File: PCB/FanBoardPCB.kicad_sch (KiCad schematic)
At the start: 0 parts

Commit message: yippeeeeee
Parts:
- added C1, C2: 100uF, Capacitor_SMD:C_0805_2012Metric, symbol Device:C
- added D1, D2, D3, D4: D, symbol Device:D
- added H1, H2, H3, H4: MountingHole, MountingHole:MountingHole_3mm, symbol Mechanical:MountingHole
- added J1: FanBrdConn, Connector_Molex:Molex_Micro-Fit_3.0_43045-0612_2x03_P3.00mm_Vertical, symbol Connector_Generic:Conn_02x03_Top_Bottom
- added J2: Fan1, UTSVT_Connectors:Molex_MicroFit3.0_1x2xP3.00mm_PolarizingPeg_Vertical, symbol Connector_Generic:Conn_02x01_Row_Letter_First
- added J3: Fan2, UTSVT_Connectors:Molex_MicroFit3.0_1x2xP3.00mm_PolarizingPeg_Vertical, symbol Connector_Generic:Conn_02x01_Row_Letter_First
- added J4: Fan3, UTSVT_Connectors:Molex_MicroFit3.0_1x2xP3.00mm_PolarizingPeg_Vertical, symbol Connector_Generic:Conn_02x01_Row_Letter_First
- added J5: Fan4, UTSVT_Connectors:Molex_MicroFit3.0_1x2xP3.00mm_PolarizingPeg_Vertical, symbol Connector_Generic:Conn_02x01_Row_Letter_First
- added LED1: SMLMN2BCTT86C, blue_led:LEDM2012X100N, symbol led:SMLMN2BCTT86C
- added Q1, Q2, Q3, Q4: IRLML0030, Package_TO_SOT_SMD:SOT-23, symbol Transistor_FET:IRLML0030
- added R1, R2, R3, R4, R5, R6, R7, R8: R100k, Resistor_SMD:R_0805_2012Metric, symbol Device:R
- added R9: R1k, Resistor_SMD:R_0805_2012Metric, symbol Device:R
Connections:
- new net: D1.2 (A), J2.a1 (Pin_a1), Q1.3 (D)
- new net: Q4.1 (G), R7.2, R8.2
- new net: D4.2 (A), J5.a1 (Pin_a1), Q4.3 (D)
- new net: D3.2 (A), J4.a1 (Pin_a1), Q3.3 (D)
- new net: LED1.2 (A), R9.2
- new net: Q1.1 (G), R1.2, R2.2
- new net: Q2.1 (G), R3.2, R4.2
- new net: Q3.1 (G), R5.2, R6.2
- new net: D2.2 (A), J3.a1 (Pin_a1), Q2.3 (D)
- new net +12V: C1.1, C2.1, D1.1 (K), D2.1 (K), D3.1 (K), D4.1 (K), J1.1 (Pin_1), J2.b1 (Pin_b1), J3.b1 (Pin_b1), J4.b1 (Pin_b1), J5.b1 (Pin_b1), R9.1
- new net FAN1: J1.2 (Pin_2), R1.1
- new net FAN2: J1.3 (Pin_3), R3.1
- new net FAN3: J1.5 (Pin_5), R5.1
- new net FAN4: J1.6 (Pin_6), R7.1
- new net GND: R2.1, R4.1, R6.1, R8.1
- new net GNDPWR: C1.2, C2.2, J1.4 (Pin_4), LED1.1 (K), Q1.2 (S), Q2.2 (S), Q3.2 (S), Q4.2 (S)

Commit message: yippeee! schem fixed probably
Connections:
- net FAN1: now also R2.2
- net FAN2: now also R3.2, R4.1; no longer R3.1
- net FAN3: now also R5.2, R6.1; no longer R5.1
- net FAN4: now also R7.2, R8.1; no longer R7.1
- net GND: now also R3.1, R5.1, R7.1; no longer R4.1, R6.1, R8.1
- net at Q4.1 (G), R8.2: no longer R7.2
- net at Q1.1 (G), R1.2: no longer R2.2
- net at Q2.1 (G), R4.2: no longer R3.2
- net at Q3.1 (G), R6.2: no longer R5.2
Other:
- moved on the sheet: R2

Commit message: ishan is annoying (joke)
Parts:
- R1, R2, R3, R4, R5, R6, R7, R8: value R100k -> 100k
- R9: value R1k -> 1k
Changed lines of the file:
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@@
 			)
 		)
-		(property "Value" "R100k"
+		(property "Value" "100k"
 			(at 88.9 99.06 90)
 			(effects
@@
 			)
 		)
-		(property "Value" "R1k"
+		(property "Value" "1k"
 			(at 74.93 123.1899 0)
 			(effects
@@
 			)
 		)
-		(property "Value" "R100k"
+		(property "Value" "100k"
 			(at 133.35 110.4899 0)
 			(effects
@@
 			)
 		)
-		(property "Value" "R100k"
+		(property "Value" "100k"
 			(at 137.16 99.06 90)
 			(effects
@@
 			)
 		)
-		(property "Value" "R100k"
+		(property "Value" "100k"
 			(at 88.9 48.26 90)
 			(effects
@@
 			)
 		)
-		(property "Value" "R100k"
+		(property "Value" "100k"
 			(at 85.09 59.6899 0)
 			(effects
@@
 			)
 		)
-		(property "Value" "R100k"
+		(property "Value" "100k"
 			(at 85.09 110.4899 0)
 			(effects
@@
 			)
 		)
-		(property "Value" "R100k"
+		(property "Value" "100k"
 			(at 133.35 59.6899 0)
 			(effects
@@
 			)
 		)
-		(property "Value" "R100k"
+		(property "Value" "100k"
 			(at 137.16 48.26 90)
 			(effects

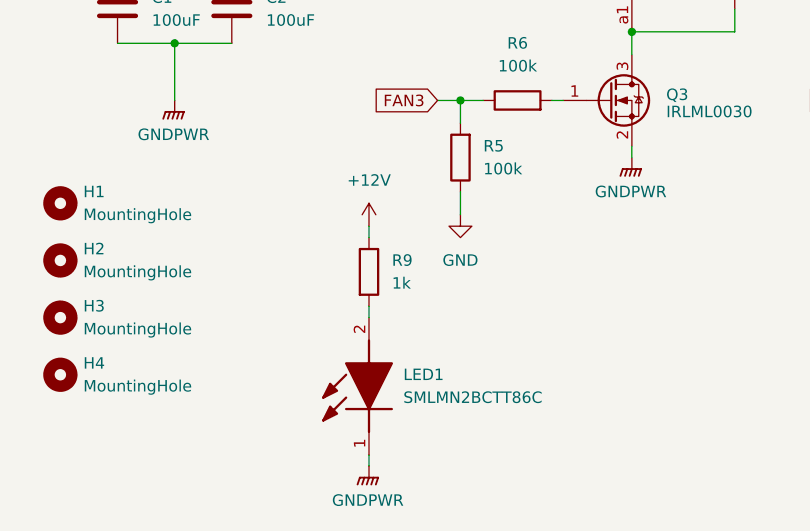
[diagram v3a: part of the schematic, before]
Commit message: adjusted led down to 5mA, still kinda a lot admittedly, 15mW for the led and 60mW for the whole circuit
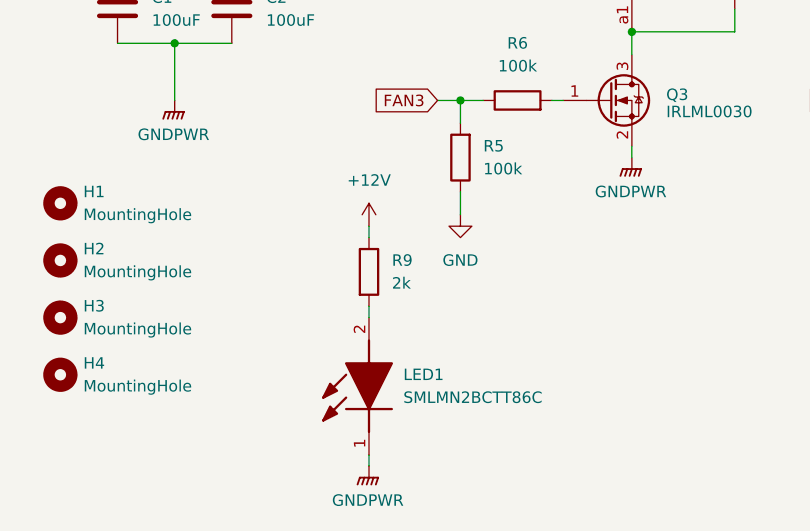
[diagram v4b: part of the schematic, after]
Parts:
- R9: value 1k -> 2k
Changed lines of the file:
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@@
 			)
 		)
-		(property "Value" "1k"
+		(property "Value" "2k"
 			(at 74.93 123.1899 0)
 			(effects

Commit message: gndpwr moment
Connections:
- net GND is gone; now on net GNDPWR: R2.1, R3.1, R5.1, R7.1

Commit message: layout (it probably sucks)
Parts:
- removed D1, D2, D3, D4: D, symbol Device:D
- removed J2: Fan1, UTSVT_Connectors:Molex_MicroFit3.0_1x2xP3.00mm_PolarizingPeg_Vertical, symbol Connector_Generic:Conn_02x01_Row_Letter_First
- removed J3: Fan2, UTSVT_Connectors:Molex_MicroFit3.0_1x2xP3.00mm_PolarizingPeg_Vertical, symbol Connector_Generic:Conn_02x01_Row_Letter_First
- removed J4: Fan3, UTSVT_Connectors:Molex_MicroFit3.0_1x2xP3.00mm_PolarizingPeg_Vertical, symbol Connector_Generic:Conn_02x01_Row_Letter_First
- removed J5: Fan4, UTSVT_Connectors:Molex_MicroFit3.0_1x2xP3.00mm_PolarizingPeg_Vertical, symbol Connector_Generic:Conn_02x01_Row_Letter_First
- removed LED1: SMLMN2BCTT86C, blue_led:LEDM2012X100N, symbol led:SMLMN2BCTT86C
- removed Q1, Q2, Q3, Q4: IRLML0030, Package_TO_SOT_SMD:SOT-23, symbol Transistor_FET:IRLML0030
- removed R1, R2, R3, R4, R5, R6, R7, R8: 100k, Resistor_SMD:R_0805_2012Metric, symbol Device:R
- added LED1: SMLMN2BCTT86C, blue_led:LEDM2012X100N, symbol Device:LED
- renumbered J1 to J5
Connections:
- net GNDPWR: now also LED1.1 (K)
- net at R9.2: now also LED1.2 (A)
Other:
- added sheet Fan_Sheet (Fan_Sheet.kicad_sch)
- moved on the sheet: R9

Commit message: something
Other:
- sheet Fan_Sheet renamed Fan_Sheet1
- added sheet Fan_Sheet2 (Fan_Sheet.kicad_sch)
- added sheet Fan_Sheet3 (Fan_Sheet.kicad_sch)
- added sheet Fan_Sheet4 (Fan_Sheet.kicad_sch)
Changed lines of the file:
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@@
+	(wire
+		(pts
+			(xy 101.6 77.47) (xy 104.14 77.47)
+		)
+		(stroke
+			(width 0)
+			(type default)
+		)
+	)
 	(wire
 		(pts
@@
 	(wire
 		(pts
+			(xy 101.6 93.98) (xy 104.14 93.98)
+		)
+		(stroke
+			(width 0)
+			(type default)
+		)
+	)
+	(wire
+		(pts
 			(xy 55.88 63.5) (xy 66.04 63.5)
+		)
+		(stroke
+			(width 0)
+			(type default)
+		)
+	)
+	(wire
+		(pts
+			(xy 101.6 110.49) (xy 104.14 110.49)
 		)
 		(stroke
@@
 	(global_label "FAN4"
 		(shape input)
-		(at 66.04 63.5 0)
+		(at 104.14 110.49 0)
 		(fields_autoplaced yes)
 		(effects
@@
 		)
 		(property "Intersheetrefs" "${INTERSHEET_REFS}"
+			(at 111.8424 110.49 0)
+			(effects
+				(font
+					(size 1.27 1.27)
+				)
+				(justify left)
+				(hide yes)
+			)
+		)
+	)
+	(global_label "FAN4"
+		(shape input)
+		(at 66.04 63.5 0)
+		(fields_autoplaced yes)
+		(effects
+			(font
+				(size 1.27 1.27)
+			)
+			(justify left)
+		)
+		(property "Intersheetrefs" "${INTERSHEET_REFS}"
 			(at 73.7424 63.5 0)
 			(effects
@@
 	(global_label "FAN3"
 		(shape input)
-		(at 66.04 60.96 0)
+		(at 104.14 93.98 0)
 		(fields_autoplaced yes)
 		(effects
@@
 		)
 		(property "Intersheetrefs" "${INTERSHEET_REFS}"
+			(at 111.8424 93.98 0)
+			(effects
+				(font
+					(size 1.27 1.27)
+				)
+				(justify left)
+				(hide yes)
+			)
+		)
+	)
+	(global_label "FAN3"
+		(shape input)
+		(at 66.04 60.96 0)
+		(fields_autoplaced yes)
+		(effects
+			(font
+				(size 1.27 1.27)
+			)
+			(justify left)
+		)
+		(property "Intersheetrefs" "${INTERSHEET_REFS}"
 			(at 73.7424 60.96 0)
+			(effects
+				(font
+					(size 1.27 1.27)
+				)
+				(justify left)
+				(hide yes)
+			)
+		)
+	)
+	(global_label "FAN2"
+		(shape input)
+		(at 104.14 77.47 0)
+		(fields_autoplaced yes)
+		(effects
+			(font
+				(size 1.27 1.27)
+			)
+			(justify left)
+		)
+		(property "Intersheetrefs" "${INTERSHEET_REFS}"
+			(at 111.8424 77.47 0)
 			(effects
 				(font
@@
 	)
 	(sheet
-		(at 80.01 57.15)
+		(at 80.01 90.17)
 		(size 21.59 10.16)
 		(fields_autoplaced yes)
@@
 			(color 0 0 0 0.0000)
 		)
-		(property "Sheetname" "Fan_Sheet"
+		(property "Sheetname" "Fan_Sheet3"
+			(at 80.01 89.4584 0)
+			(effects
+				(font
+					(size 1.27 1.27)
+				)
+				(justify left bottom)
+			)
+		)
+		(property "Sheetfile" "Fan_Sheet.kicad_sch"
+			(at 80.01 100.9146 0)
+			(effects
+				(font
+					(size 1.27 1.27)
+				)
+				(justify left top)
+			)
+		)
+		(pin "FAN_PWM" input
+			(at 101.6 93.98 0)
+			(effects
+				(font
+					(size 1.27 1.27)
+				)
+				(justify right)
+			)
+		)
+		(instances
+			(project "FanBoardPCB"
+				(path "/1aabcb47-8889-428a-a945-776d6a97cab7"
+					(page "4")
+				)
+			)
+		)
+	)
+	(sheet
+		(at 80.01 106.68)
+		(size 21.59 10.16)
+		(fields_autoplaced yes)
+		(stroke
+			(width 0.1524)
+			(type solid)
+			(color 255 173 47 1)
+		)
+		(fill
+			(color 0 0 0 0.0000)
+		)
+		(property "Sheetname" "Fan_Sheet4"
+			(at 80.01 105.9684 0)
+			(effects
+				(font
+					(size 1.27 1.27)
+				)
+				(justify left bottom)
+			)
+		)
+		(property "Sheetfile" "Fan_Sheet.kicad_sch"
+			(at 80.01 117.4246 0)
+			(effects
+				(font
+					(size 1.27 1.27)
+				)
+				(justify left top)
+			)
+		)
+		(pin "FAN_PWM" input
+			(at 101.6 110.49 0)
+			(effects
+				(font
+					(size 1.27 1.27)
+				)
+				(justify right)
+			)
+		)
+		(instances
+			(project "FanBoardPCB"
+				(path "/1aabcb47-8889-428a-a945-776d6a97cab7"
+					(page "5")
+				)
+			)
+		)
+	)
+	(sheet
+		(at 80.01 73.66)
+		(size 21.59 10.16)
+		(fields_autoplaced yes)
+		(stroke
+			(width 0.1524)
+			(type solid)
+			(color 255 173 47 1)
+		)
+		(fill
+			(color 0 0 0 0.0000)
+		)
+		(property "Sheetname" "Fan_Sheet2"
+			(at 80.01 72.9484 0)
+			(effects
+				(font
+					(size 1.27 1.27)
+				)
+				(justify left bottom)
+			)
+		)
+		(property "Sheetfile" "Fan_Sheet.kicad_sch"
+			(at 80.01 84.4046 0)
+			(effects
+				(font
+					(size 1.27 1.27)
+				)
+				(justify left top)
+			)
+		)
+		(pin "FAN_PWM" input
+			(at 101.6 77.47 0)
+			(effects
+				(font
+					(size 1.27 1.27)
+				)
+				(justify right)
+			)
+		)
+		(instances
+			(project "FanBoardPCB"
+				(path "/1aabcb47-8889-428a-a945-776d6a97cab7"
+					(page "3")
+				)
+			)
+		)
+	)
+	(sheet
+		(at 80.01 57.15)
+		(size 21.59 10.16)
+		(fields_autoplaced yes)
+		(stroke
+			(width 0.1524)
+			(type solid)
+			(color 255 173 47 1)
+		)
+		(fill
+			(color 0 0 0 0.0000)
+		)
+		(property "Sheetname" "Fan_Sheet1"
 			(at 80.01 56.4384 0)
 			(effects

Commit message: fixed
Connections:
- net +12V: now also LED1.2 (A); no longer R9.1
- net GNDPWR: now also R9.2; no longer LED1.1 (K)
- new net: LED1.1 (K), R9.1
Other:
- moved on the sheet: LED1, R9
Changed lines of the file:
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@@
+	(wire
+		(pts
+			(xy 101.6 77.47) (xy 104.14 77.47)
+		)
+		(stroke
+			(width 0)
+			(type default)
+		)
+	)
+	(wire
+		(pts
+			(xy 50.8 88.9) (xy 44.45 88.9)
+		)
+		(stroke
+			(width 0)
+			(type default)
+		)
+	)
+	(wire
+		(pts
+			(xy 101.6 93.98) (xy 104.14 93.98)
+		)
+		(stroke
+			(width 0)
+			(type default)
+		)
+	)
+	(wire
+		(pts
+			(xy 55.88 63.5) (xy 66.04 63.5)
+		)
+		(stroke
+			(width 0)
+			(type default)
+		)
+	)
+	(wire
+		(pts
+			(xy 101.6 110.49) (xy 104.14 110.49)
+		)
+		(stroke
+			(width 0)
+			(type default)
+		)
+	)
+	(wire
+		(pts
+			(xy 34.29 60.96) (xy 43.18 60.96)
+		)
+		(stroke
+			(width 0)
+			(type default)
+		)
+	)
+	(wire
+		(pts
+			(xy 55.88 60.96) (xy 66.04 60.96)
+		)
+		(stroke
+			(width 0)
+			(type default)
+		)
+	)
+	(wire
+		(pts
+			(xy 40.64 55.88) (xy 40.64 58.42)
+		)
+		(stroke
+			(width 0)
+			(type default)
+		)
+	)
+	(wire
+		(pts
+			(xy 50.8 88.9) (xy 57.15 88.9)
+		)
+		(stroke
+			(width 0)
+			(type default)
+		)
+	)
+	(wire
+		(pts
+			(xy 58.42 66.04) (xy 58.42 58.42)
+		)
+		(stroke
+			(width 0)
+			(type default)
+		)
+	)
 	(wire
 		(pts
@@
 	(wire
 		(pts
-			(xy 101.6 77.47) (xy 104.14 77.47)
+			(xy 50.8 83.82) (xy 50.8 88.9)
+		)
+		(stroke
+			(width 0)
+			(type default)
+		)
+	)
+	(wire
+		(pts
+			(xy 58.42 58.42) (xy 55.88 58.42)
+		)
+		(stroke
+			(width 0)
+			(type default)
+		)
+	)
+	(wire
+		(pts
+			(xy 34.29 63.5) (xy 43.18 63.5)
+		)
+		(stroke
+			(width 0)
+			(type default)
+		)
+	)
+	(wire
+		(pts
+			(xy 101.6 60.96) (xy 104.14 60.96)
 		)
 		(stroke
@@
 	(wire
 		(pts
-			(xy 50.8 88.9) (xy 44.45 88.9)
-		)
-		(stroke
-			(width 0)
-			(type default)
-		)
-	)
-	(wire
-		(pts
-			(xy 101.6 93.98) (xy 104.14 93.98)
-		)
-		(stroke
-			(width 0)
-			(type default)
-		)
-	)
-	(wire
-		(pts
-			(xy 55.88 63.5) (xy 66.04 63.5)
-		)
-		(stroke
-			(width 0)
-			(type default)
-		)
-	)
-	(wire
-		(pts
-			(xy 101.6 110.49) (xy 104.14 110.49)
-		)
-		(stroke
-			(width 0)
-			(type default)
-		)
-	)
-	(wire
-		(pts
-			(xy 34.29 60.96) (xy 43.18 60.96)
-		)
-		(stroke
-			(width 0)
-			(type default)
-		)
-	)
-	(wire
-		(pts
-			(xy 55.88 60.96) (xy 66.04 60.96)
-		)
-		(stroke
-			(width 0)
-			(type default)
-		)
-	)
-	(wire
-		(pts
-			(xy 40.64 55.88) (xy 40.64 58.42)
-		)
-		(stroke
-			(width 0)
-			(type default)
-		)
-	)
-	(wire
-		(pts
-			(xy 50.8 88.9) (xy 57.15 88.9)
-		)
-		(stroke
-			(width 0)
-			(type default)
-		)
-	)
-	(wire
-		(pts
-			(xy 58.42 66.04) (xy 58.42 58.42)
-		)
-		(stroke
-			(width 0)
-			(type default)
-		)
-	)
-	(wire
-		(pts
-			(xy 50.8 83.82) (xy 50.8 88.9)
-		)
-		(stroke
-			(width 0)
-			(type default)
-		)
-	)
-	(wire
-		(pts
-			(xy 58.42 58.42) (xy 55.88 58.42)
-		)
-		(stroke
-			(width 0)
-			(type default)
-		)
-	)
-	(wire
-		(pts
-			(xy 34.29 63.5) (xy 43.18 63.5)
-		)
-		(stroke
-			(width 0)
-			(type default)
-		)
-	)
-	(wire
-		(pts
-			(xy 101.6 60.96) (xy 104.14 60.96)
+			(xy 43.18 58.42) (xy 40.64 58.42)
+		)
+		(stroke
+			(width 0)
+			(type default)
+		)
+	)
+	(wire
+		(pts
+			(xy 50.8 96.52) (xy 50.8 102.87)
+		)
+		(stroke
+			(width 0)
+			(type default)
+		)
+	)
+	(wire
+		(pts
+			(xy 50.8 96.52) (xy 57.15 96.52)
+		)
+		(stroke
+			(width 0)
+			(type default)
+		)
+	)
+	(wire
+		(pts
+			(xy 44.45 96.52) (xy 50.8 96.52)
 		)
 		(stroke
@@
 		(pts
 			(xy 59.69 142.24) (xy 59.69 143.51)
-		)
-		(stroke
-			(width 0)
-			(type default)
-		)
-	)
-	(wire
-		(pts
-			(xy 43.18 58.42) (xy 40.64 58.42)
-		)
-		(stroke
-			(width 0)
-			(type default)
-		)
-	)
-	(wire
-		(pts
-			(xy 50.8 96.52) (xy 50.8 102.87)
-		)
-		(stroke
-			(width 0)
-			(type default)
-		)
-	)
-	(wire
-		(pts
-			(xy 50.8 96.52) (xy 57.15 96.52)
-		)
-		(stroke
-			(width 0)
-			(type default)
-		)
-	)
-	(wire
-		(pts
-			(xy 44.45 96.52) (xy 50.8 96.52)
 		)
 		(stroke
@@
 	(symbol
 		(lib_id "Device:R")
-		(at 59.69 129.54 0)
+		(at 59.69 138.43 0)
 		(unit 1)
 		(exclude_from_sim no)
@@
 		(fields_autoplaced yes)
 		(property "Reference" "R9"
-			(at 62.23 128.2699 0)
+			(at 62.23 137.1599 0)
 			(effects
 				(font
@@
 		)
 		(property "Value" "2k"
-			(at 62.23 130.8099 0)
+			(at 62.23 139.6999 0)
 			(effects
 				(font
@@
 		)
 		(property "Footprint" "Resistor_SMD:R_0805_2012Metric"
-			(at 57.912 129.54 90)
+			(at 57.912 138.43 90)
 			(effects
 				(font
@@
 		)
 		(property "Datasheet" "~"
-			(at 59.69 129.54 0)
+			(at 59.69 138.43 0)
 			(effects
 				(font
@@
 		)
 		(property "Description" "Resistor"
-			(at 59.69 129.54 0)
+			(at 59.69 138.43 0)
 			(effects
 				(font
@@
 	(symbol
 		(lib_id "Device:LED")
-		(at 59.69 138.43 90)
+		(at 59.69 129.54 90)
 		(unit 1)
 		(exclude_from_sim no)
@@
 		(fields_autoplaced yes)
 		(property "Reference" "LED1"
-			(at 63.5 138.7474 90)
+			(at 63.5 129.8574 90)
 			(effects
 				(font
@@
 		)
 		(property "Value" "SMLMN2BCTT86C"
-			(at 63.5 141.2874 90)
+			(at 63.5 132.3974 90)
 			(effects
 				(font
@@
 		)
 		(property "Footprint" "blue_led:LEDM2012X100N"
-			(at 59.69 138.43 0)
+			(at 59.69 129.54 0)
 			(effects
 				(font
@@
 		)
 		(property "Datasheet" "https://fscdn.rohm.com/en/products/databook/datasheet/opto/led/chip_mono/smlmn2bctt86(c)-e.pdf"
-			(at 59.69 138.43 0)
+			(at 59.69 129.54 0)
 			(effects
 				(font
@@
 		)
 		(property "Description" "Light emitting diode"
-			(at 59.69 138.43 0)
+			(at 59.69 129.54 0)
 			(effects
 				(font
@@
 		)
 		(property "mouser part" "755-SMLMN2BCTT86C"
-			(at 59.69 138.43 90)
-			(effects
-				(font
+			(at 59.69 129.54 90)
+			(effects
+				(font
